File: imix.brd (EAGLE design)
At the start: 87 x 102.5 mm, 159 parts, among them IC1 AD712R, Q1 AO3418, Q2 AO3415, Q3 AO3415, Q5 AO3415, Q6 AO3415, U1 BQ2423X, U10 LDO-TPS78233, U11 ATSAM4LCX_100, U3 NRF51822, U4 BAL_NRF01D3, U6 FX0S8700CQ, U7 SI7021, U8 ISL29035, X1 16MHz, X2 16MHz, X4 16MHz

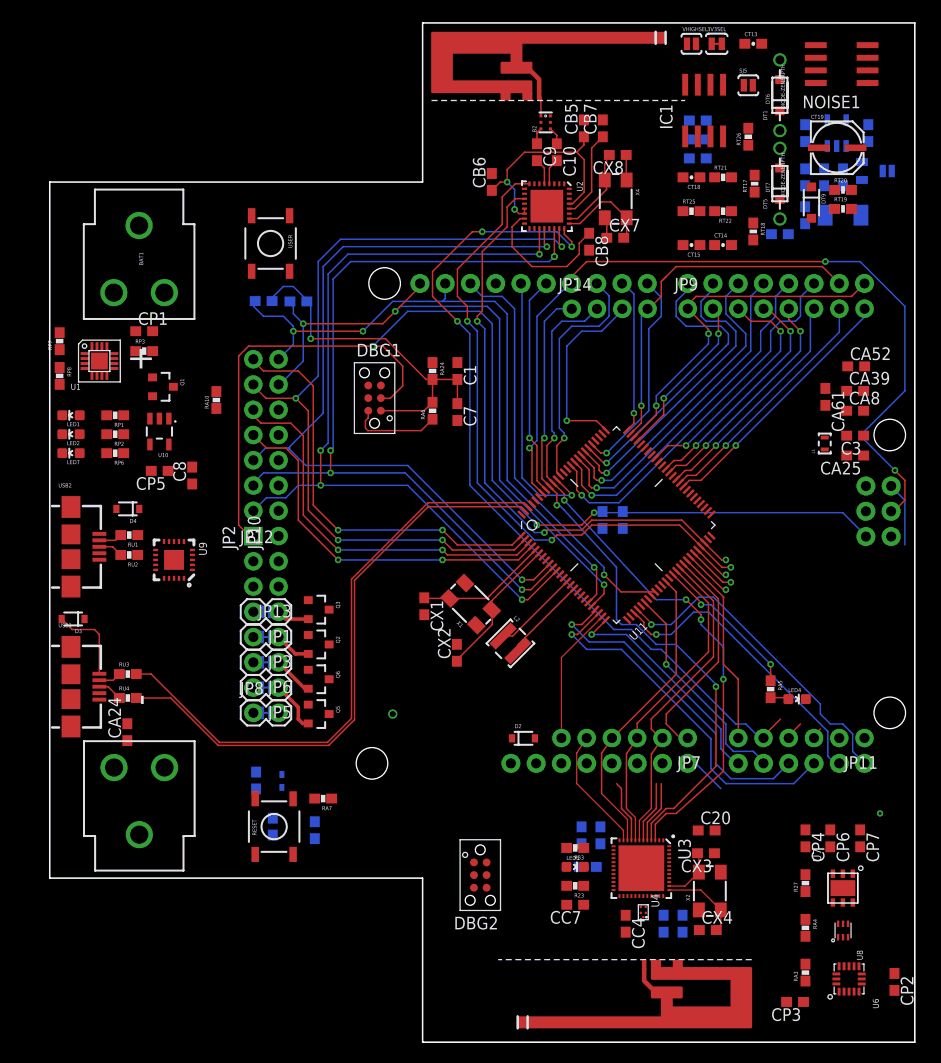
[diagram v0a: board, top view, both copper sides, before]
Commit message: More routing in lower right quadrant
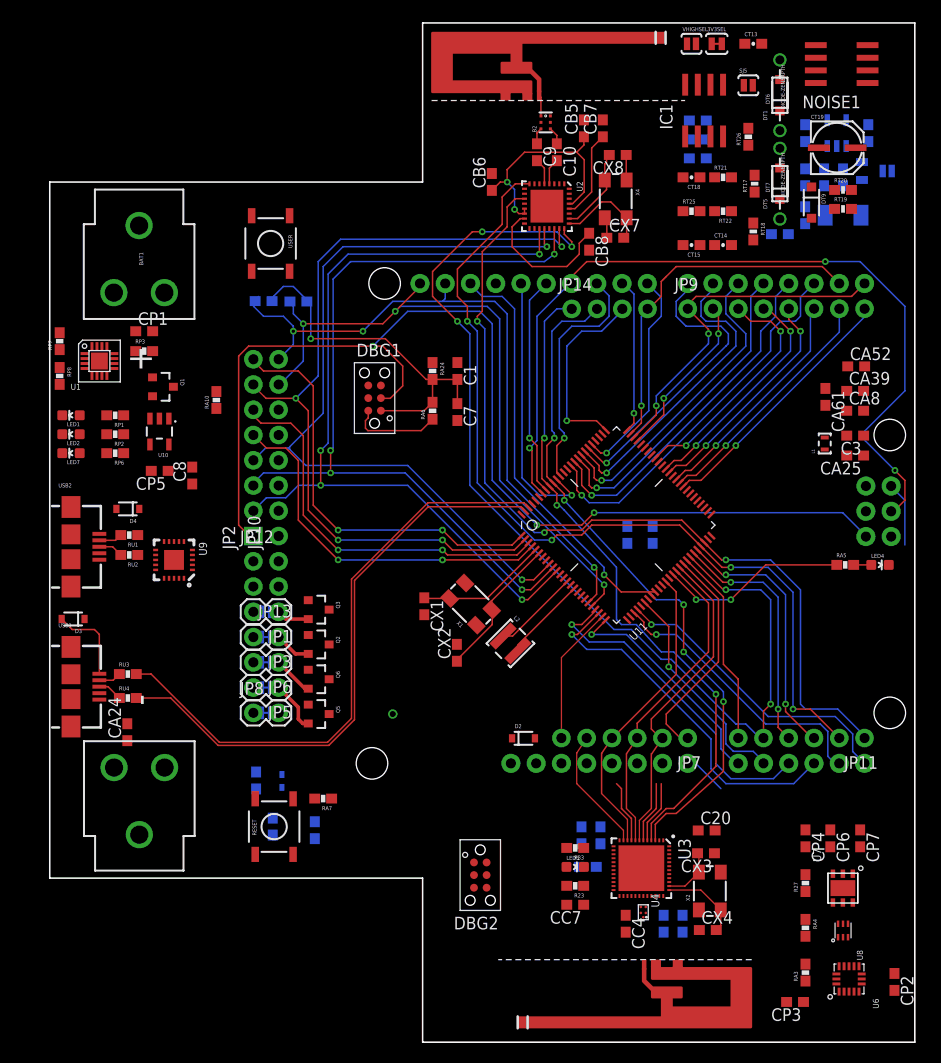
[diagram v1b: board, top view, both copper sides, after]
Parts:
- moved LED4 15.9 mm to (83.5, 31.5)
- moved RA5 14.6 mm to (80.0, 31.5), turned to 0 degrees
- moved CA5 3.35 mm to (60.6, 34.5)
- moved C2 2.92 mm to (58.1, 34.5)
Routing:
- net RF233_SLP: track 60.3 -> 88.5 mm
- net RF233_!RST: track 65.0 -> 89.9 mm, vias 3 -> 4
- net NRF_SWDIO: track 5.09 -> 26.5 mm, vias 1 -> 2
- net USART3_RTS: track 6.83 -> 24.9 mm, vias 1 -> 2
- net RF233_IRQ: track 89.1 -> 105.6 mm, vias 4 -> 5
- net USER_LED: track 15.4 -> 19.1 mm
- net ADCIFE5: track 33.2 -> 30.3 mm
- net ADCIFE4: track 30.5 -> 28.7 mm
- net TWI2_SCL: track 68.0 -> 67.5 mm
- net MOSI: track 82.2 -> 82.0 mm, vias 5 -> 4
- net ACC_INT2: vias 1 -> 0

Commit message: Progress on routing
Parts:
- removed DBG1, DBG2: JTAG_6-PIN_NEEDLE, stanford_iot_research:JTAG_6-PIN_NEEDLE
- added TC1, TC2: TC2030-IDC, TagConnect:TC2030-IDC
- moved CA24 52.6 mm to (59.7, 23.3), turned to 270 degrees
- moved CA52 40.0 mm to (43.1, 39.0)
- moved CA61 37.7 mm to (46.3, 28.1), turned to 315 degrees
- moved RA4 35.4 mm to (84.0, 29.5), turned to 180 degrees
- moved C3 34.7 mm to (56.0, 20.5)
- moved RA6 30.2 mm to (48.5, 18.5), turned to 0 degrees
- moved RA24 27.2 mm to (44.5, 24.5), turned to 225 degrees
- moved CA8 27.0 mm to (54.0, 48.0)
- moved C1 26.3 mm to (16.5, 41.5), turned to 90 degrees
- moved CA39 24.8 mm to (59.3, 37.0), flipped to the bottom, turned to 90 degrees
- moved CP7 23.6 mm to (84.0, 27.5), turned to 0 degrees
- moved U7 23.4 mm to (82.5, 22.3), turned to 0 degrees
- moved C7 18.4 mm to (37.0, 28.9), turned to 225 degrees
- moved RA10 17.2 mm to (30.0, 59.0), turned to 270 degrees
- moved CP3 15.0 mm to (84.0, -0.50), turned to 0 degrees
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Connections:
- net !RESET: now also TC2.3; no longer DBG1.!RESET
- net GND: now also TC1.5, TC2.5; no longer DBG1.GND, DBG2.GND
- net NRF_SWDCLK: now also TC1.4; no longer DBG2.SWCLK
- net NRF_SWDIO: now also TC1.2; no longer DBG2.SWDIO
- net SWDCLK/TCK: now also TC2.4; no longer DBG1.SWCLK
- net SWDIO/TMS: now also TC2.2; no longer DBG1.SWDIO
- net VCC_3V3: no longer 3V3SEL.2, CT14.1, RT22.2, RT25.2, RT26.1
- net VCC_MCU_3V3: now also TC2.1; no longer DBG1.VTREF
- net VCC_NRF_3V3: now also TC1.1; no longer DBG2.VTREF
- net VCC_TRNG_3V3: now also 3V3SEL.2, CT14.1, RT22.2, RT25.2, RT26.1
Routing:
- net NRF_GPIO: track 6.32 -> 129.9 mm, vias 0 -> 14
- net EXTINT1: track 0.00 -> 111.2 mm, vias 0 -> 5
- net VCC_TRNG_3V3: track 0.00 -> 105.4 mm, vias 0 -> 6
- net NRF_SWDCLK: track 16.9 -> 120.9 mm, vias 2 -> 7
- net USART3_RTS: track 24.9 -> 125.8 mm, vias 2 -> 9
- net VCC_SENSE_3V3: track 0.00 -> 91.5 mm, vias 0 -> 4
- net USER_BTN: track 0.00 -> 81.7 mm, vias 0 -> 3
- net VCC_MCU_3V3: track 191.1 -> 111.7 mm, vias 2 -> 6
- net !NRF_PWR_EN: track 24.7 -> 101.6 mm, vias 1 -> 6
- net USER_LED: track 19.1 -> 96.0 mm, vias 2 -> 5
- net !SENSE_PWR_EN: track 26.1 -> 97.0 mm, vias 1 -> 6
- net GND: track 0.00 -> 70.3 mm, vias 0 -> 35
- net TWI2_SDA: track 69.1 -> 133.6 mm, vias 5 -> 9
- net VHIGH: track 0.00 -> 64.2 mm, vias 0 -> 5
- net TRNG_OUT: track 23.1 -> 83.3 mm
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- added copper zone on layer 1, net GND
- added copper zone on layer 15, net VCC_NRF_3V3
- added copper zone on layer 15, net VCC_SENSE_3V3
- added copper zone on layer 15, net VCC_TRNG_3V3
- removed copper zone on layer 15, net VCC_MCU_3V3
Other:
- board text added: "AT86RF233"
- board text added: "ATSAM4LC8"
- board text added: "IMIX v2 June 2016 Shane Leonard"
- board text added: "NRF51822"
- board text added: "POWER MEASURE"
- board text added: "SENSORS"
- board text added: "TRNG"

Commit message: Fully routed and some silkscreen finished
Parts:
- JP2: device SparkFun-Connectors:1X08_PIN1_NO_SILK -> SparkFun-Connectors:1X08_NO_SILK
- moved CA5 29.8 mm to (45.2, 20.8), flipped to the top, turned to 315 degrees
- moved C2 27.4 mm to (46.8, 22.2), flipped to the top, turned to 315 degrees
- moved D2 17.3 mm to (35.1, 2.06)
- moved RP8 12.2 mm to (12.5, 54.5), turned to 0 degrees
- moved RP7 8.02 mm to (9.00, 53.5), turned to 0 degrees
- moved CA25 4.43 mm to (68.2, 37.8), flipped to the top, turned to 90 degrees
- moved C3 4.24 mm to (59.0, 23.5)
- moved RA6 4.03 mm to (52.5, 19.0), turned to 315 degrees
- moved RP3 4.03 mm to (7.50, 49.5), turned to 270 degrees
- moved CP7 4.00 mm to (80.0, 27.5), turned to 180 degrees
- moved RA4 4.00 mm to (80.0, 29.5)
- moved CP1 3.91 mm to (12.5, 52.5), turned to 0 degrees
- moved C1 2.55 mm to (17.0, 39.0)
- moved C8 2.50 mm to (15.0, 39.0)
- moved CA24 1.95 mm to (59.0, 21.5), turned to 180 degrees
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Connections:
- removed net AGND: CX7.1, CX8.1, X4.CASE@2, X4.CASE@4
- new net VCC: CP5.1, Q1.2, U10.5
- net GND: now also CX7.1, CX8.1, X4.CASE@2, X4.CASE@4
- net VCC_3V3: no longer CP5.1, Q1.2, U10.5
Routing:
- net GND: track 70.3 -> 159.2 mm, vias 35 -> 58
- net VCC_EXT_5V: track 2.59 -> 78.4 mm
- net VCC_IN: track 22.7 -> 95.9 mm, vias 5 -> 4
- net VCC_3V3: track 29.2 -> 94.8 mm, vias 2 -> 3
- net VCC_MCU_3V3: track 111.7 -> 163.1 mm, vias 6 -> 9
- net N$10: track 0.00 -> 29.1 mm
- net TWI2_SCL: track 112.6 -> 126.6 mm, vias 11 -> 10
- net VCC_BAT: track 0.00 -> 13.8 mm
- net VCC: track 0.00 -> 9.29 mm
- net AGND: track 7.93 -> 0.00 mm
- net VCC_SENSE_3V3: track 91.5 -> 98.1 mm, vias 4 -> 5
- net N$48: track 9.23 -> 4.70 mm
- net VCC_TRNG_3V3: track 105.4 -> 101.9 mm
- net N$53: track 3.10 -> 6.40 mm
- net !RF233_PWR_EN: track 77.0 -> 79.9 mm
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- added copper zone on layer 16, net GND
- added copper zone on layer 15, net VCC_3V3
- added copper zone on layer 15, net VCC_MCU_3V3
- added copper zone on layer 15, net VCC_RF233_3V3

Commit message: Top silkscreen nearly complete
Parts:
- removed CA25, CB5, CB6: 100nF, rcl:C0603
- removed CT13, CT14, CT15, CT18: (no value), SparkFun-Capacitors:0603-CAP
- removed D4: NSR1020MW2T3G, SparkFun-DiscreteSemi:SOD-323
- removed JP7: (no value), SparkFun-Connectors:1X06_NO_SILK
- removed RA6, RA7, RA8: 10K, SparkFun-Passives:0603-RES
- removed RT20: (no value), SparkFun-Resistors:0603-RES
- removed RT25: (no value), SparkFun-Passives:0603-RES
- removed RU2: 27, SparkFun-Passives:0603-RES
- added C17, C21, C30, C33: 100nF, rcl:C0603
- added C18: 10uF, rcl:C0603
- added C25: 4.7uF, rcl:C0603
- added C26: 6.8uF, rcl:C0603
- added D9: NSR1020MW2T3G, SparkFun-DiscreteSemi:SOD-323
- added JP15: (no value), SparkFun-Connectors:1X08_NO_SILK
- added R13: (no value), SparkFun-Resistors:0603-RES
- added R34: 1K, SparkFun-Passives:0603-RES
- added R35, R36: 10K, SparkFun-Passives:0603-RES
- added R37: 4.7K, SparkFun-Passives:0603-RES
- added R8: (no value), SparkFun-Passives:0603-RES
- added U$2, U$3, U$5, U$6: FIDUCIAL, GeekAmmo:FIDUCIAL
- C1: value 10uF -> 100nF
- C10, C9: value 22pF -> (none); device rcl:C0603 -> SparkFun-Capacitors:0603-CAP
- C2: value 6.8uF -> 22pF
- C3: value 4.7uF -> 22pF
- C7, C8: value 100nF -> (none); device rcl:C0603 -> SparkFun-Capacitors:0603-CAP
- R23: value 10K -> 27
- R27: value 4.7K -> 10K
- R32: value 1K -> 10K
- moved C4 70.2 mm to (53.0, 73.0)
- moved C7 63.5 mm to (70.5, 84.0), turned to 0 degrees
- moved C8 58.4 mm to (64.5, 70.0), turned to 180 degrees
- moved R23 55.8 mm to (8.00, 32.5)
- moved C2 50.8 mm to (49.0, 73.0), turned to 270 degrees
- moved C3 50.1 mm to (51.0, 73.0), turned to 270 degrees
- moved C1 45.3 mm to (47.0, 73.0)
- moved D2 44.4 mm to (7.86, 37.1), turned to 180 degrees
- moved R27 34.3 mm to (52.5, 19.0), turned to 315 degrees
- moved C20 32.8 mm to (68.2, 37.8), turned to 90 degrees
- moved R33 21.7 mm to (33.5, 5.00), turned to 90 degrees
- moved R32 20.5 mm to (31.5, 5.00)
- moved C10 18.8 mm to (68.0, 65.0), turned to 0 degrees
- moved C9 18.3 mm to (64.5, 63.2), turned to 180 degrees
- moved U8 0.50 mm to (78.8, 4.78)
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- renumbered CA24 to C27, CA39 to C50, CA5 to C28, CA52 to C19, CA61 to C22, CA8 to C15, CB7 to C5, CB8 to C13, CC2 to C32, CC3 to C31, CC4 to C37, CC5 to C38, CC6 to C35, CC7 to C36, CFF to C11, CP1 to C14, CP2 to C41, CP3 to C42, CP4 to C43, CP5 to C16, CP6 to C40, CP7 to C29, CT11 to C45, CT12 to C44, CT16 to C47, CT17 to C48, CT19 to C49, CT6 to C46, CX1 to C23, CX2 to C24, CX3 to C34, CX4 to C39, CX7 to C12, CX8 to C6, DT1 to D1, RA1 to R1, RA10 to R3, RA2 to R2, RA24 to R26, RA3 to R38, RA4 to R25, RA5 to R24, RA9 to R31, RP1 to R19, RP2 to R20, RP3 to R18, RP6 to R21, RP7 to R16, RP8 to R17, RT17 to R6, RT18 to R10, RT19 to R9, RT21 to R5, RT22 to R7, RT26 to R4, RT28 to R14, RT29 to R15, RT30 to R11, RT31 to R12, RU1 to R22, RU3 to R28, RU4 to R29
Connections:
- net ACC_INT1: now also JP15.1; no longer JP7.1
- net GND: now also C1.2, C10.2, C17.2, C18.1, C21.2, C25.2, C26.2, C30.2, C33.2, JP15.7, JP15.8, R13.1; no longer C1.1, C2.2, C3.2, C8.2, CA25.2, CB5.2, CB6.2, CT13.2, CT14.2, RT20.1
- net LIGHT_!INT: now also JP15.6, R37.1; no longer JP7.6, R27.1
- net N$1: now also C2.2; no longer C9.2
- net N$10: now also C20.1, C25.1; no longer C3.1, CA25.1
- net N$12: now also C26.1; no longer C2.1
- net N$17: now also C3.2; no longer C10.2
- net N$2: now also C1.1, C4.1; no longer CB5.1, CB6.1
- net N$22: now also C2.1; no longer C9.1
- net N$26: now also R23.2; no longer RU2.2
- net N$30: now also R23.1; no longer RU2.1
- net N$41: now also C3.1; no longer C10.1
- net N$75: now also R34.2; no longer R32.2
- net N$8: now also C30.1, R33.1; no longer C4.1, RA8.1
- net NOISE1: now also C9.1; no longer CT15.1
- net NOISE2: now also C8.1, R13.2; no longer CT18.1, RT20.2
- net NRF_LED: now also R34.1; no longer R32.1
- net NRF_SWDCLK: now also R36.1; no longer R33.1
- net NRF_SWDIO: now also R35.1; no longer R23.1
- net SWDCLK/TCK: now also R32.1; no longer RA7.1
- net SWDIO/TMS: now also R27.1; no longer RA6.1
- net TRNG_OUT: now also C8.2, C9.2, R8.1; no longer CT15.2, CT18.2, RT25.1
- net USART2_CTS: now also JP15.4; no longer JP7.4
- net USART2_RTS: now also JP15.5; no longer JP7.5
- net USART2_RX: now also JP15.3; no longer JP7.3
- net USART2_TX: now also JP15.2; no longer JP7.2
- net VCC_3V3: now also C17.1; no longer C8.1
- net VCC_DBG_USB_5V: now also D2.A; no longer D4.A
- net VCC_EXT_5V: now also D9.A; no longer D2.A
- net VCC_IN: now also D9.C; no longer D4.C
- net VCC_MCU_3V3: now also C18.2, C21.1, R27.2, R32.2, R33.2; no longer C1.2, C7.1, RA6.2, RA7.2, RA8.2
- net VCC_NRF_3V3: now also C33.1, R35.2, R36.2; no longer C20.1, R23.2, R33.2
- net VCC_SENSE_3V3: now also R37.2; no longer R27.2
- net VCC_TRNG_3V3: now also C10.1, R8.2; no longer CT14.1, RT25.2
- net VHIGH: now also C7.1; no longer CT13.1
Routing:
- net VCC_3V3: track 94.8 -> 84.1 mm
- net VCC_SENSE_3V3: track 98.1 -> 91.2 mm
- net NRF_GPIO: track 130.8 -> 134.4 mm
- net VCC_MCU_3V3: track 163.1 -> 166.0 mm
- net TWI2_SDA: track 134.1 -> 131.4 mm
- net GND: track 159.2 -> 156.6 mm, vias 58 -> 61
- net RF233_SLP: track 90.5 -> 88.6 mm
- net TWI1_SCL: track 67.1 -> 68.5 mm
- net NRF_INT: track 75.9 -> 74.6 mm
- net GPIO7: track 30.5 -> 29.2 mm
- net NOISE2: track 42.5 -> 41.3 mm
- net RF233_!RST: track 92.5 -> 91.5 mm
- net TWI2_SCL: track 126.6 -> 127.5 mm
- net VCC_NRF_3V3: track 51.0 -> 51.8 mm
- net VCC_TRNG_3V3: track 101.9 -> 102.7 mm
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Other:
- board text added: "!CHG"
- board text added: "!CS0"
- board text added: "!CS1"
- board text added: "!CS2"
- board text added: "!CS3"
- board text added: "!NRF_EN"
- board text added: "!NRF_RST"
- board text added: "!RF233_EN"
- board text added: "!RST"
- board text added: "!SENSE_EN"
- board text added: "3V3"
- board text added: "3V3SEL"
- board text added: "5V"
- board text added: "AREF"
- board text added: "BQ2324X"
- board text added: "C1"
- board text added: "C10"
- board text added: "C11"
- board text added: "C12"
- board text added: "C13"
- board text added: "C14"
- board text added: "C15"
- board text added: "C16"
- board text added: "C17"
- board text added: "C18"
- board text added: "C19"
- board text added: "C2"
- board text added: "C20"
- board text added: "C21"
- board text added: "C22"
- board text added: "C23"
- board text added: "C24"
- board text added: "C25"
- board text added: "C26"
- board text added: "C27"
- board text added: "C28"
- board text added: "C29"
- board text added: "C3"
- board text added: "C30"
- board text added: "C31"
- board text added: "C32"
- board text added: "C33"
- board text added: "C34"
- board text added: "C35"
- board text added: "C36"
- board text added: "C37"
- board text added: "C38"
- board text added: "C39"
- board text added: "C4"
- board text added: "C40"
- board text added: "C41"
- board text added: "C42"
- board text added: "C43"
- board text added: "C49"
- board text added: "C5"
- board text added: "C6"
- board text added: "C7"
- board text added: "C8"
- board text added: "C9"
- board text added: "CLK0"
- board text added: "CLK2"
- board text added: "CTS0"
- board text added: "D2"
- board text added: "D3"
- board text added: "D4"
- board text added: "D5"
- board text added: "D6"
- board text added: "D7"
- board text added: "D8"
- board text added: "D9"
- board text added: "DEBUG"
- board text added: "EXTINT1"
- board text added: "FT0"
- board text added: "FT1"
- board text added: "FT2"
- board text added: "FT231X"
- board text added: "FT3"
- board text added: "GND"
- board text added: "IC1"
- board text added: "ISL29035"
- board text added: "L1"
- board text added: "L2"
- board text added: "MCU"
- board text added: "MCU SWD"
- board text added: "MISO"
- board text added: "MOSI"
- board text added: "NOISE1"
- board text added: "NRF"
- board text added: "NRF SWD"
- board text added: "NRF_GPIO"
- board text added: "NRF_INT"
- board text added: "Q1"
- board text added: "Q2"
- board text added: "Q3"
- board text added: "Q5"
- board text added: "Q6"
- board text added: "R1"
- board text added: "R10"
- board text added: "R11"
- board text added: "R12"
- board text added: "R13"
- board text added: "R16"
- board text added: "R17"
- board text added: "R18"
- board text added: "R19"
- board text added: "R2"
- board text added: "R20"
- board text added: "R21"
- board text added: "R22"
- board text added: "R23"
- board text added: "R24"
- board text added: "R25"
- board text added: "R26"
- board text added: "R27"
- board text added: "R28"
- board text added: "R29"
- board text added: "R3"
- board text added: "R31"
- board text added: "R32"
- board text added: "R33"
- board text added: "R34"
- board text added: "R35"
- board text added: "R36"
- board text added: "R37"
- board text added: "R38"
- board text added: "R4"
- board text added: "R5"
- board text added: "R6"
- board text added: "R7"
- board text added: "R8"
- board text added: "R9"
- board text added: "RESET"
- board text added: "RF233"
- board text added: "RTS0"
- board text added: "RX0"
- board text added: "RX3"
- board text added: "SCK"
- board text added: "SCL1"
- board text added: "SCL2"
- board text added: "SDA1"
- board text added: "SDA2"
- board text added: "SI7021"
- board text added: "SJ5"
- board text added: "TRNG_EN"
- board text added: "TRNG_OUT"
- board text added: "TX0"
- board text added: "TX3"
- board text added: "U10"
- board text added: "USER"
- board text added: "USER_BTN"
- board text added: "USER_LED"
- board text added: "VHIGHSEL"
- board text added: "X1"
- board text added: "X2"
- board text added: "X4"
